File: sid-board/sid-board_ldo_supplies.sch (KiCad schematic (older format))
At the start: 18 parts, among them J1 ICM_CONN, J2 SID_CONN, J3 5V OUT, J4 3.3V OUT, J5 SPI, SW1 SW_DIP_x02, U1 SC16IS752IPW, U2 MCP1703A-3302_SOT223, U3 PCA82C250, U4 PCA82C250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

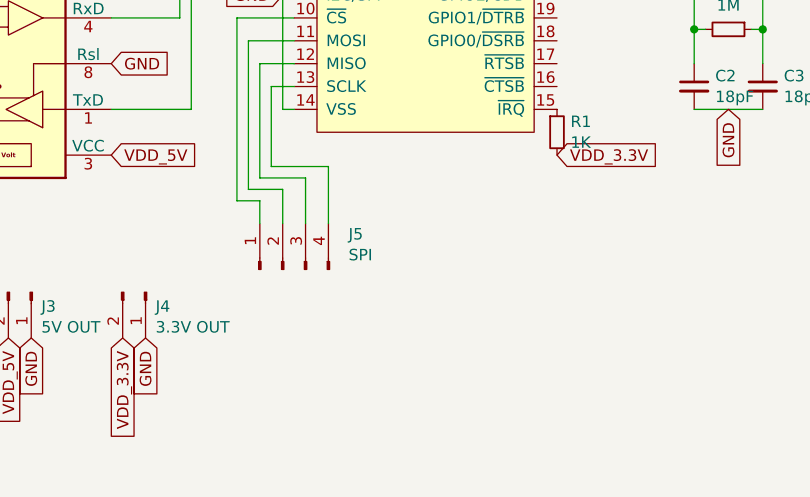
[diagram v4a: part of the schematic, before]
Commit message: Added TODO text about putting interrupt connection back.
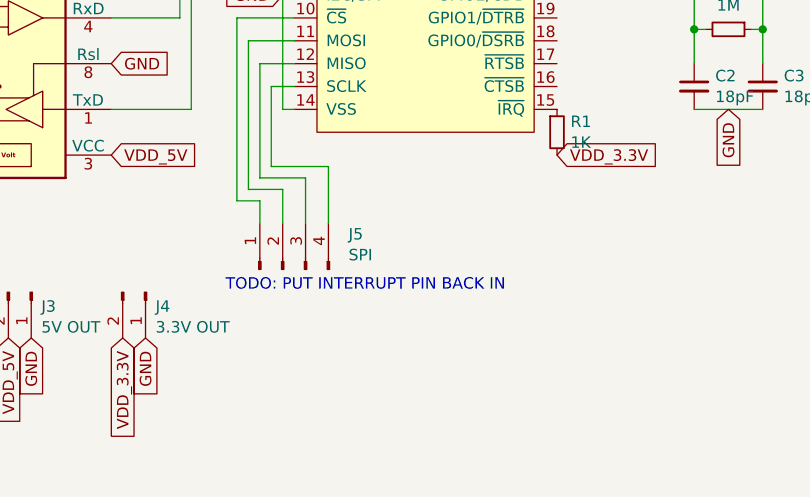
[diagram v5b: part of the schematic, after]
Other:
- note added: "TODO: PUT INTERRUPT PIN BACK IN"
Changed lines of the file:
@@
 Wire Wire Line
 	2850 3700 3900 3700
+Text Notes 5200 4500 0    50   ~ 0
+TODO: PUT INTERRUPT PIN BACK IN
 $EndSCHEMATC

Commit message: FINAL BEFORE FABRICATION!
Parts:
- J5: value SPI -> SPI/INT; footprint Connector_PinHeader_2.54mm:PinHeader_1x04_P2.54mm_Vertical -> Connector_PinHeader_2.54mm:PinHeader_1x05_P2.54mm_Vertical; symbol Connector:Conn_01x04_Male -> Connector:Conn_01x05_Male
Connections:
- wire segments 70 -> 71
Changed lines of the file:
@@
 EESchema Schematic File Version 4
+LIBS:sid-board_ldo_supplies-cache
 EELAYER 30 0
 EELAYER END
@@
 	5500 3600 5400 3600
 Wire Wire Line
-	5400 3600 5400 3950
-Wire Wire Line
-	5400 3950 5650 3950
-Wire Wire Line
-	5650 3950 5650 4200
-Wire Wire Line
 	5500 3500 5350 3500
 Wire Wire Line
-	5350 3500 5350 4000
-Wire Wire Line
-	5350 4000 5550 4000
-Wire Wire Line
-	5550 4000 5550 4200
-Wire Wire Line
 	5500 3400 5300 3400
 Wire Wire Line
-	5300 3400 5300 4050
-Wire Wire Line
-	5300 4050 5450 4050
-Wire Wire Line
-	5450 4050 5450 4200
-Wire Wire Line
 	5500 3300 5250 3300
-Wire Wire Line
-	5250 3300 5250 4100
-Wire Wire Line
-	5250 4100 5350 4100
-Wire Wire Line
-	5350 4100 5350 4200
-$Comp
-L Connector:Conn_01x04_Male J5
+$Comp
+L Connector:Conn_01x05_Male J5
 U 1 1 5E308950
 P 5450 4400
 F 0 "J5" V 5604 4112 50  0000 R CNN
-F 1 "SPI" V 5513 4112 50  0000 R CNN
-F 2 "Connector_PinHeader_2.54mm:PinHeader_1x04_P2.54mm_Vertical" H 5450 4400 50  0001 C CNN
+F 1 "SPI/INT" V 5513 4112 50  0000 R CNN
+F 2 "Connector_PinHeader_2.54mm:PinHeader_1x05_P2.54mm_Vertical" H 5450 4400 50  0001 C CNN
 F 3 "~" H 5450 4400 50  0001 C CNN
 	1    5450 4400
@@
 Text Notes 5200 4500 0    50   ~ 0
 TODO: PUT INTERRUPT PIN BACK IN
+Wire Wire Line
+	5250 3300 5250 4200
+Wire Wire Line
+	5300 4200 5350 4200
+Wire Wire Line
+	5300 3400 5300 4200
+Wire Wire Line
+	5350 4150 5450 4150
+Wire Wire Line
+	5450 4150 5450 4200
+Wire Wire Line
+	5350 3500 5350 4150
+Wire Wire Line
+	5400 4100 5550 4100
+Wire Wire Line
+	5550 4100 5550 4200
+Wire Wire Line
+	5400 3600 5400 4100
+Wire Wire Line
+	5650 4200 5650 4050
+Wire Wire Line
+	5650 4050 6800 4050
+Wire Wire Line
+	6800 4050 6800 3700
+Wire Wire Line
+	6800 3700 6650 3700
+Connection ~ 6650 3700
 $EndSCHEMATC
